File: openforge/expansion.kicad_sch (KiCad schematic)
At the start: 23 parts, among them P10 YL004-030-001, P8 Female Header 2x23Pin 2.54MM, P9 Female Header 2x23Pin 2.54MM, U7 24LC32AT-I/OT

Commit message: added footprint associations
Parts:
- R13, R15, R150, R151, R152, R153, R154, R155, R156, R157, R16, R2, R31, R32: footprint (none) -> Resistor_SMD:R_0402_1005Metric
- TP4: footprint (none) -> TestPoint:TestPoint_Pad_1.5x1.5mm
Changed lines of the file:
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@@
 			)
 		)
-		(property "Footprint" ""
+		(property "Footprint" "Resistor_SMD:R_0402_1005Metric"
 			(at 108.712 173.99 90)
 			(effects
@@
 			)
 		)
-		(property "Footprint" ""
+		(property "Footprint" "Resistor_SMD:R_0402_1005Metric"
 			(at 62.23 187.198 90)
 			(effects
@@
 			)
 		)
-		(property "Footprint" ""
+		(property "Footprint" "Resistor_SMD:R_0402_1005Metric"
 			(at 85.852 173.99 90)
 			(effects
@@
 			)
 		)
-		(property "Footprint" ""
+		(property "Footprint" "TestPoint:TestPoint_Pad_1.5x1.5mm"
 			(at 314.96 203.2 0)
 			(effects
@@
 			)
 		)
-		(property "Footprint" ""
+		(property "Footprint" "Resistor_SMD:R_0402_1005Metric"
 			(at 97.282 173.99 90)
 			(effects
@@
 			)
 		)
-		(property "Footprint" ""
+		(property "Footprint" "Resistor_SMD:R_0402_1005Metric"
 			(at 62.23 192.278 90)
 			(effects
@@
 			)
 		)
-		(property "Footprint" ""
+		(property "Footprint" "Resistor_SMD:R_0402_1005Metric"
 			(at 62.23 204.978 90)
 			(effects
@@
 			)
 		)
-		(property "Footprint" ""
+		(property "Footprint" "Resistor_SMD:R_0402_1005Metric"
 			(at 101.092 173.99 90)
 			(effects
@@
 			)
 		)
-		(property "Footprint" ""
+		(property "Footprint" "Resistor_SMD:R_0402_1005Metric"
 			(at 89.662 173.99 90)
 			(effects
@@
 			)
 		)
-		(property "Footprint" ""
+		(property "Footprint" "Resistor_SMD:R_0402_1005Metric"
 			(at 104.902 173.99 90)
 			(effects
@@
 			)
 		)
-		(property "Footprint" ""
+		(property "Footprint" "Resistor_SMD:R_0402_1005Metric"
 			(at 62.23 189.738 90)
 			(effects
@@
 			)
 		)
-		(property "Footprint" ""
+		(property "Footprint" "Resistor_SMD:R_0402_1005Metric"
 			(at 62.23 202.438 90)
 			(effects
@@
 			)
 		)
-		(property "Footprint" ""
+		(property "Footprint" "Resistor_SMD:R_0402_1005Metric"
 			(at 62.23 197.358 90)
 			(effects
@@
 			)
 		)
-		(property "Footprint" ""
+		(property "Footprint" "Resistor_SMD:R_0402_1005Metric"
 			(at 318.262 181.61 90)
 			(effects
@@
 			)
 		)
-		(property "Footprint" ""
+		(property "Footprint" "Resistor_SMD:R_0402_1005Metric"
 			(at 93.472 173.99 90)
 			(effects

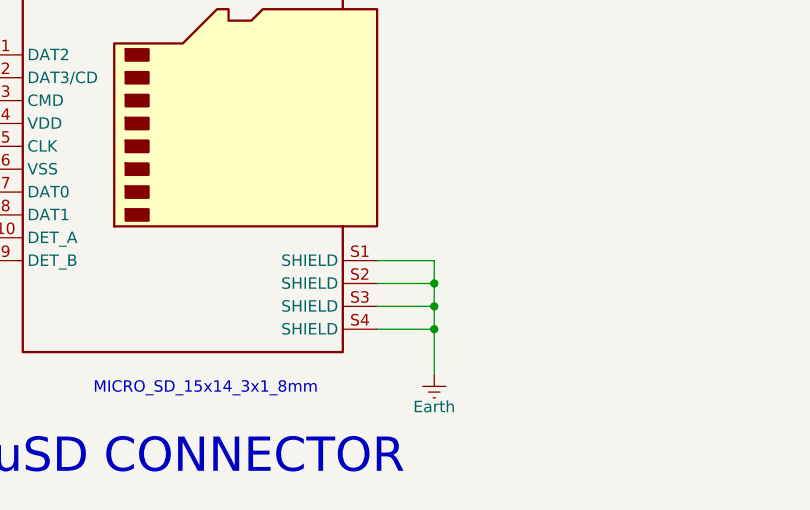
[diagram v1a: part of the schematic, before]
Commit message: Completed footprint association. Partially placed top side components on PCB
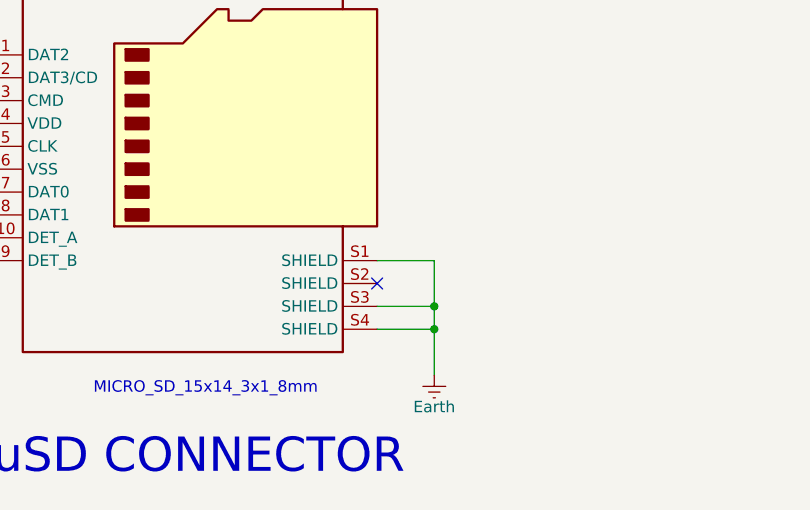
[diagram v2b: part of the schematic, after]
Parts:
- P10: footprint (none) -> footprints:yl004-030-001
- P8, P9: footprint Connector_PinSocket_2.54mm:PinSocket_2x23_P2.54mm_Vertical -> Connector_PinHeader_2.54mm:PinHeader_2x23_P2.54mm_Vertical
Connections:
- net Earth: no longer P10.S2 (SHIELD)
- no-connect marks 0 -> 1
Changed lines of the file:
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@@
 	)
 	(junction
-		(at 175.26 210.82)
-		(diameter 0)
-		(color 0 0 0 0)
-	)
-	(junction
 		(at 91.44 158.75)
 		(diameter 0)
@@
 		(color 0 0 0 0)
 	)
+	(no_connect
+		(at 168.91 210.82)
+	)
 	(wire
 		(pts
@@
 	(wire
 		(pts
-			(xy 175.26 210.82) (xy 175.26 213.36)
+			(xy 175.26 208.28) (xy 175.26 213.36)
 		)
 		(stroke
@@
 	(wire
 		(pts
-			(xy 175.26 208.28) (xy 175.26 210.82)
-		)
-		(stroke
-			(width 0)
-			(type default)
-		)
-	)
-	(wire
-		(pts
 			(xy 308.61 72.39) (xy 349.25 72.39)
 		)
@@
 	(wire
 		(pts
-			(xy 168.91 210.82) (xy 175.26 210.82)
-		)
-		(stroke
-			(width 0)
-			(type default)
-		)
-	)
-	(wire
-		(pts
 			(xy 255.27 87.63) (xy 295.91 87.63)
 		)
@@
 			)
 		)
-		(property "Footprint" "Connector_PinSocket_2.54mm:PinSocket_2x23_P2.54mm_Vertical"
+		(property "Footprint" "Connector_PinHeader_2.54mm:PinHeader_2x23_P2.54mm_Vertical"
 			(at 111.76 82.55 0)
 			(effects
@@
 			)
 		)
-		(property "Footprint" ""
+		(property "Footprint" "footprints:yl004-030-001"
 			(at 200.66 177.8 0)
 			(effects
@@
 			)
 		)
-		(property "Footprint" "Connector_PinSocket_2.54mm:PinSocket_2x23_P2.54mm_Vertical"
+		(property "Footprint" "Connector_PinHeader_2.54mm:PinHeader_2x23_P2.54mm_Vertical"
 			(at 300.99 82.55 0)
 			(effects

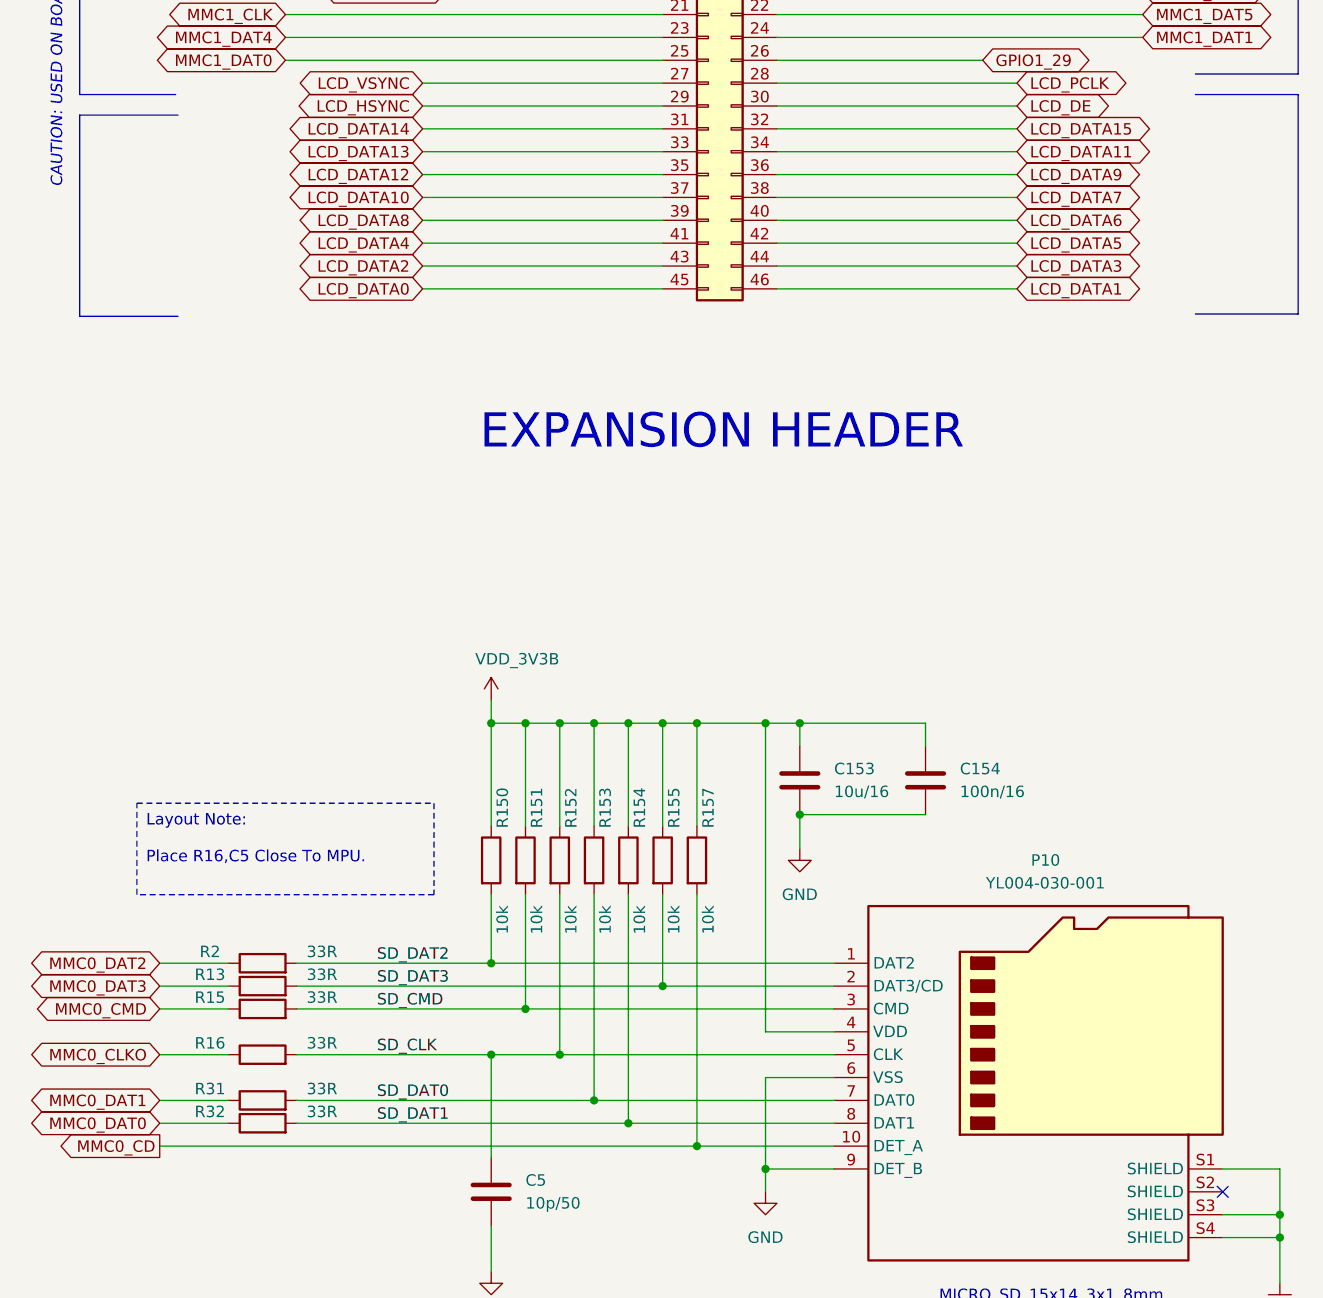
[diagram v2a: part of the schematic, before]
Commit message: PCB all layers copied from beaglebone black
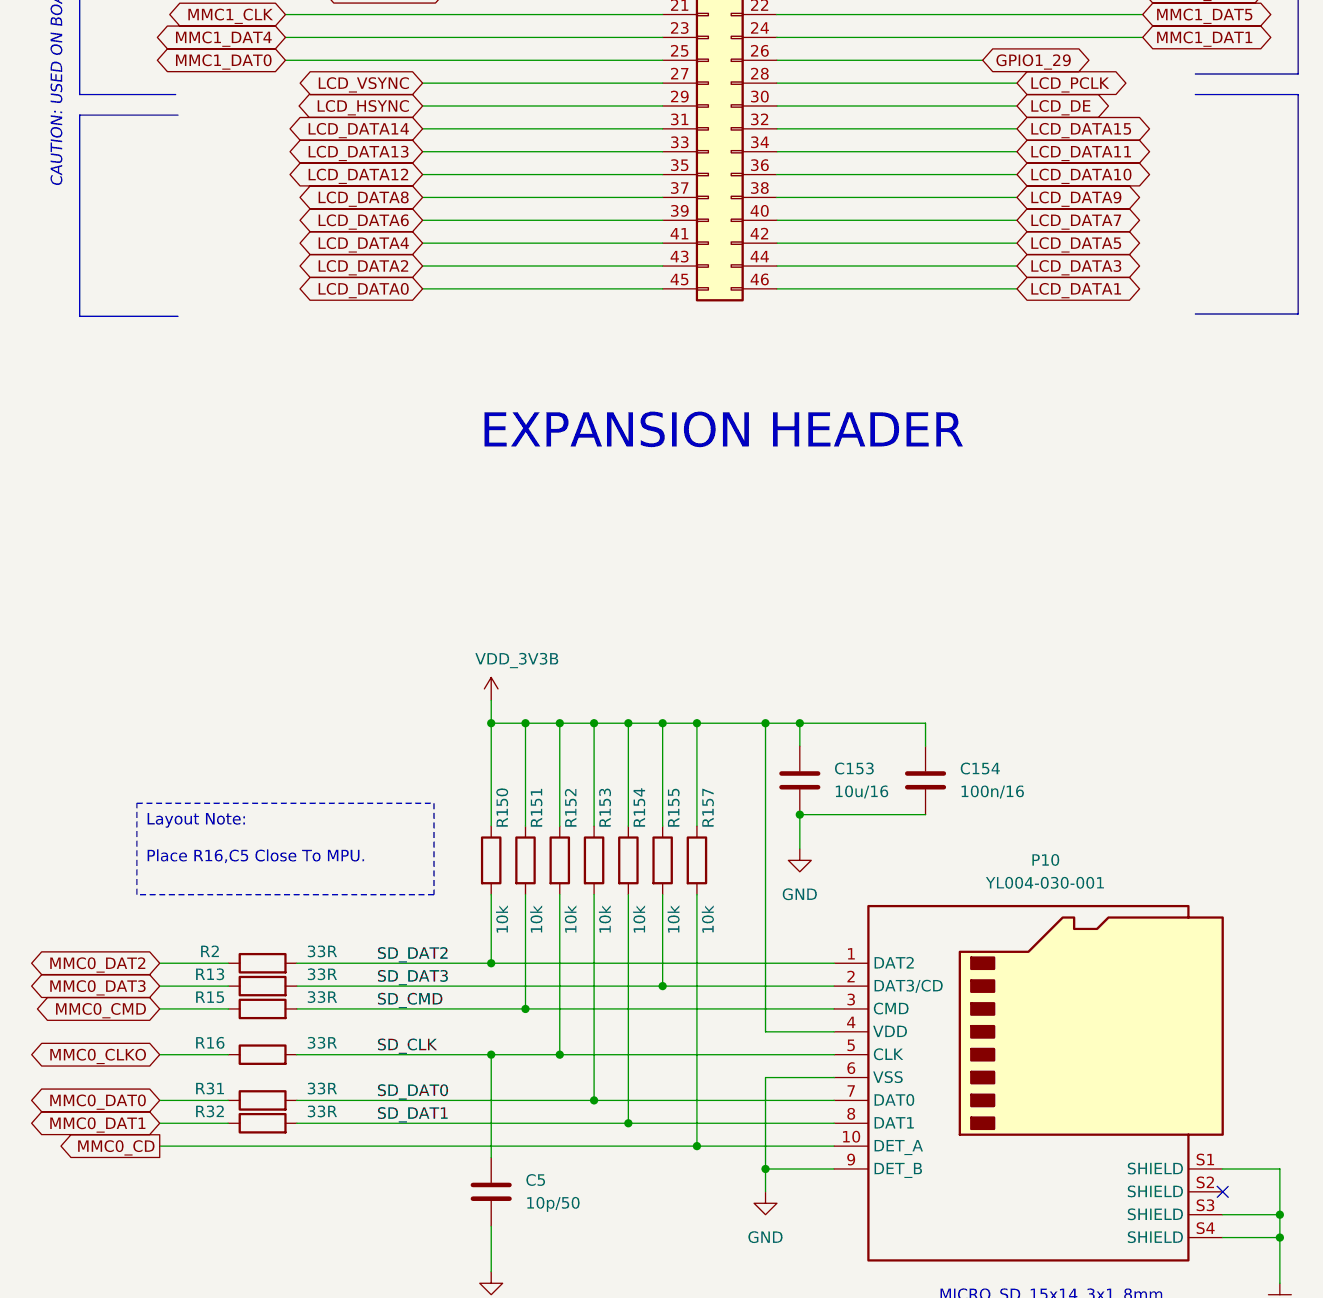
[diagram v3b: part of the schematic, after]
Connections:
- net LCD_DATA10: now also P8.36 (Pin_36); no longer P8.37 (Pin_37)
- net LCD_DATA6: now also P8.39 (Pin_39); no longer P8.40 (Pin_40)
- net LCD_DATA7: now also P8.40 (Pin_40); no longer P8.38 (Pin_38)
- net LCD_DATA8: now also P8.37 (Pin_37); no longer P8.39 (Pin_39)
- net LCD_DATA9: now also P8.38 (Pin_38); no longer P8.36 (Pin_36)
- net MMC0_DAT0: now also R31.1; no longer R32.1
- net MMC0_DAT1: now also R32.1; no longer R31.1

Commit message: fixed various footprints
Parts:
- TP4: footprint TestPoint:TestPoint_Pad_1.5x1.5mm -> TestPoint:TestPoint_Pad_D1.0mm
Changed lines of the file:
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@@
 			)
 		)
-		(property "Footprint" "TestPoint:TestPoint_Pad_1.5x1.5mm"
+		(property "Footprint" "TestPoint:TestPoint_Pad_D1.0mm"
 			(at 314.96 203.2 0)
 			(effects

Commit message: fixed all errors and major warnings
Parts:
- C152, C154, C5: footprint Capacitor_SMD:C_0402_1005Metric -> footprints:C_0402_1005Metric
- C153: footprint Capacitor_SMD:C_0805_2012Metric -> footprints:C_0805_2012Metric
- R13, R15, R150, R151, R152, R153, R154, R155, R156, R157, R16, R2, R31, R32: footprint Resistor_SMD:R_0402_1005Metric -> footprints:R_0402_1005Metric
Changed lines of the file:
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@@
 			)
 		)
-		(property "Footprint" "Capacitor_SMD:C_0805_2012Metric"
+		(property "Footprint" "footprints:C_0805_2012Metric"
 			(at 122.8852 168.91 0)
 			(effects
@@
 			)
 		)
-		(property "Footprint" "Capacitor_SMD:C_0402_1005Metric"
+		(property "Footprint" "footprints:C_0402_1005Metric"
 			(at 88.5952 214.63 0)
 			(effects
@@
 			)
 		)
-		(property "Footprint" "Resistor_SMD:R_0402_1005Metric"
+		(property "Footprint" "footprints:R_0402_1005Metric"
 			(at 108.712 173.99 90)
 			(effects
@@
 			)
 		)
-		(property "Footprint" "Resistor_SMD:R_0402_1005Metric"
+		(property "Footprint" "footprints:R_0402_1005Metric"
 			(at 62.23 187.198 90)
 			(effects
@@
 			)
 		)
-		(property "Footprint" "Resistor_SMD:R_0402_1005Metric"
+		(property "Footprint" "footprints:R_0402_1005Metric"
 			(at 85.852 173.99 90)
 			(effects
@@
 			)
 		)
-		(property "Footprint" "Capacitor_SMD:C_0402_1005Metric"
+		(property "Footprint" "footprints:C_0402_1005Metric"
 			(at 332.4352 185.42 0)
 			(effects
@@
 			)
 		)
-		(property "Footprint" "Resistor_SMD:R_0402_1005Metric"
+		(property "Footprint" "footprints:R_0402_1005Metric"
 			(at 97.282 173.99 90)
 			(effects
@@
 			)
 		)
-		(property "Footprint" "Resistor_SMD:R_0402_1005Metric"
+		(property "Footprint" "footprints:R_0402_1005Metric"
 			(at 62.23 192.278 90)
 			(effects
@@
 			)
 		)
-		(property "Footprint" "Resistor_SMD:R_0402_1005Metric"
+		(property "Footprint" "footprints:R_0402_1005Metric"
 			(at 62.23 204.978 90)
 			(effects
@@
 			)
 		)
-		(property "Footprint" "Capacitor_SMD:C_0402_1005Metric"
+		(property "Footprint" "footprints:C_0402_1005Metric"
 			(at 136.8552 168.91 0)
 			(effects
@@
 			)
 		)
-		(property "Footprint" "Resistor_SMD:R_0402_1005Metric"
+		(property "Footprint" "footprints:R_0402_1005Metric"
 			(at 101.092 173.99 90)
 			(effects
@@
 			)
 		)
-		(property "Footprint" "Resistor_SMD:R_0402_1005Metric"
+		(property "Footprint" "footprints:R_0402_1005Metric"
 			(at 89.662 173.99 90)
 			(effects
@@
 			)
 		)
-		(property "Footprint" "Resistor_SMD:R_0402_1005Metric"
+		(property "Footprint" "footprints:R_0402_1005Metric"
 			(at 104.902 173.99 90)
 			(effects
@@
 			)
 		)
-		(property "Footprint" "Resistor_SMD:R_0402_1005Metric"
+		(property "Footprint" "footprints:R_0402_1005Metric"
 			(at 62.23 189.738 90)
 			(effects
@@
 			)
 		)
-		(property "Footprint" "Resistor_SMD:R_0402_1005Metric"
+		(property "Footprint" "footprints:R_0402_1005Metric"
 			(at 62.23 202.438 90)
 			(effects
@@
 			)
 		)
-		(property "Footprint" "Resistor_SMD:R_0402_1005Metric"
+		(property "Footprint" "footprints:R_0402_1005Metric"
 			(at 62.23 197.358 90)
 			(effects
@@
 			)
 		)
-		(property "Footprint" "Resistor_SMD:R_0402_1005Metric"
+		(property "Footprint" "footprints:R_0402_1005Metric"
 			(at 318.262 181.61 90)
 			(effects
@@
 			)
 		)
-		(property "Footprint" "Resistor_SMD:R_0402_1005Metric"
+		(property "Footprint" "footprints:R_0402_1005Metric"
 			(at 93.472 173.99 90)
 			(effects
